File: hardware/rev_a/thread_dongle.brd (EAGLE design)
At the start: 26 x 14 mm, 26 parts, among them J1 USB-A-MALE-PLUG, J2 TC2030-JLINK-NL, U2 ESDR0502N, U3 CP2102, Y1 FH1600015

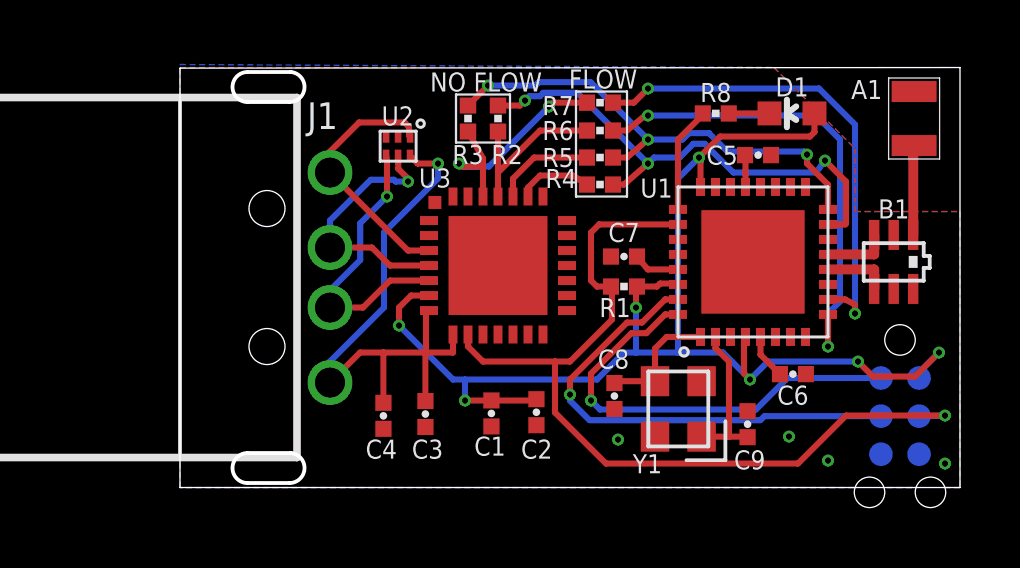
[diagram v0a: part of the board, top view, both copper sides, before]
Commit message: smaller board, cheaper uart bridge
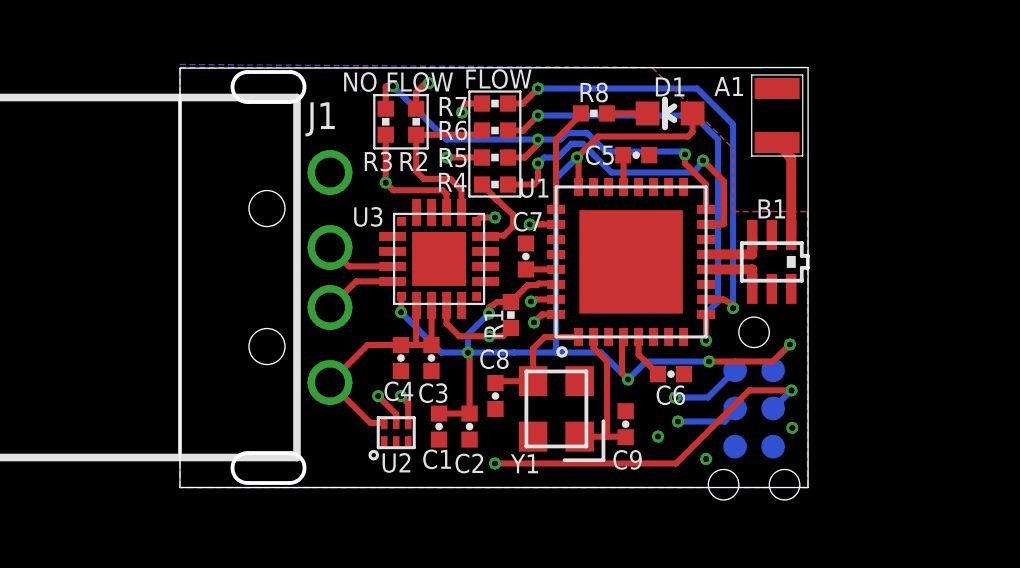
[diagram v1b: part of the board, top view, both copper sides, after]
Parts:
- U3: value CP2102 -> CP2102N-20; device silabs:MLP28 -> chips:QFN-20-3MM
- moved U2 9.55 mm to (7.21, 1.83), turned to 90 degrees
- moved J2 4.87 mm to (19.1, 2.63)
- moved A1 4.57 mm to (19.9, 11.2)
- moved C9 4.06 mm to (14.9, 2.11)
- moved U1 4.06 mm to (15.0, 7.52)
- moved B1 4.06 mm to (19.7, 7.52)
- moved C5 4.06 mm to (15.2, 11.1)
- moved C6 4.06 mm to (16.4, 3.78)
- moved D1 4.06 mm to (16.3, 12.5)
- moved R8 4.06 mm to (13.8, 12.5)
- moved Y1 4.06 mm to (12.5, 2.62)
- moved C8 3.96 mm to (10.5, 3.05)
- moved R1 3.89 mm to (11.0, 5.75), turned to 90 degrees
- moved R7 3.50 mm to (10.5, 12.8)
- moved R4 3.50 mm to (10.5, 10.1)
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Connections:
- net GND: now also U3.12, U3.P$1; no longer U3.EXP, U3.M
- net SAM_CTS: now also U3.16; no longer U3.24
- net SAM_RTS: now also U3.15; no longer U3.23
- net SAM_RX: now also U3.18; no longer U3.26
- net SAM_TX: now also U3.17; no longer U3.25
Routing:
- net N$6: track 19.7 -> 8.91 mm, vias 1 -> 0
- net GND: track 8.52 -> 0.00 mm, vias 4 -> 3
- net VCC: track 44.2 -> 37.7 mm
- net !RESET: track 29.4 -> 24.4 mm, vias 1 -> 4
- net SWDIO: track 14.8 -> 10.8 mm, vias 1 -> 2
- net SWCLK: track 16.1 -> 12.5 mm, vias 1 -> 2
- net N$4: track 9.52 -> 7.37 mm
- net SAM_CTS: track 3.36 -> 4.50 mm, vias 0 -> 2
- net SER2_P3: track 16.3 -> 15.4 mm
- net SER2_P0: track 16.2 -> 15.4 mm
- net SAM_RTS: track 2.52 -> 3.31 mm
- net SER2_P1: track 16.3 -> 15.5 mm
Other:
- board size 26 x 14 mm -> 20.9 x 14 mm
- board text removed: "U3"

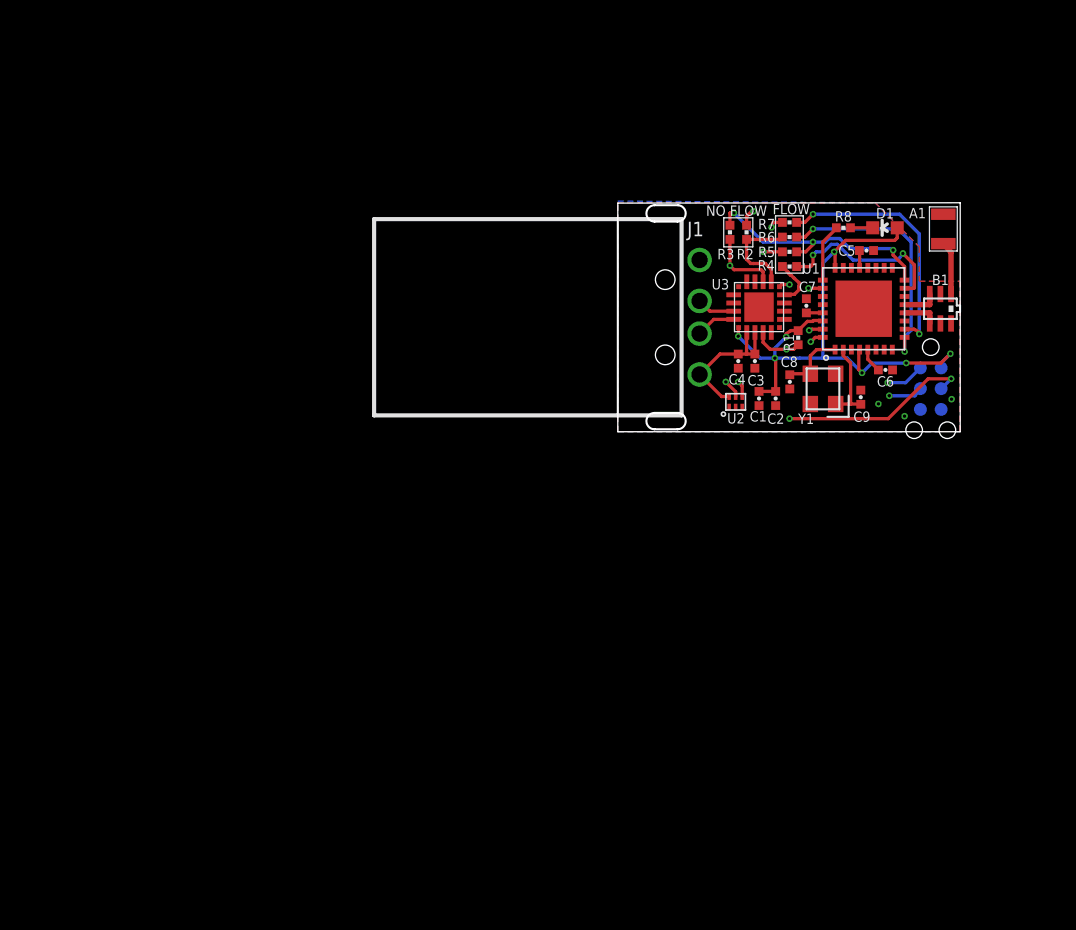
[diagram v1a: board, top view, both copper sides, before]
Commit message: Update with KW21Z instead of SAMR21
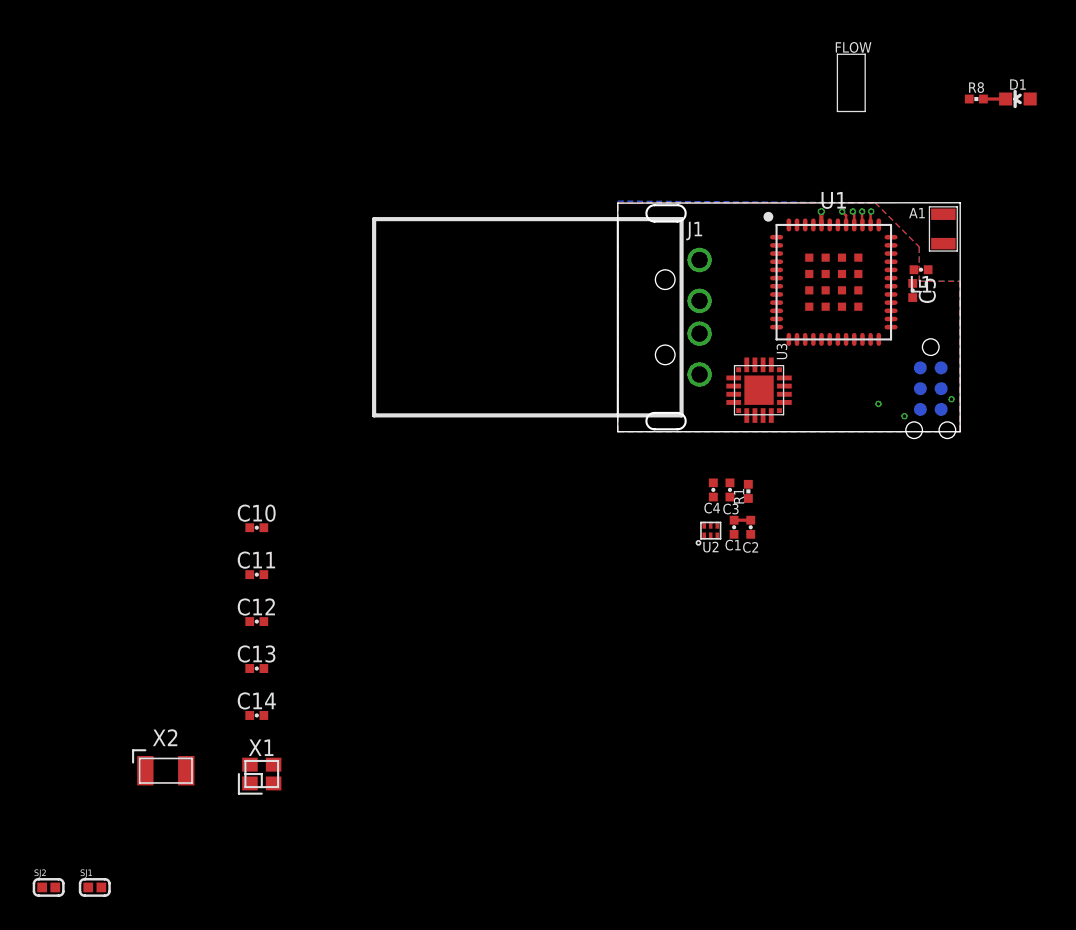
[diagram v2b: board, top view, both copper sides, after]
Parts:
- removed B1: 2450BM15A0015, chips:2450BM
- removed C6: 0.1uF, passives:0402_CAP
- removed C7: 1.0uF, passives:0402_CAP
- removed C8, C9: 8pF, passives:0402_CAP
- removed R2, R3, R4, R5, R6, R7: 0, passives:0402_RES
- removed Y1: FH1600015, crystals:FHXXX
- added C10, C11, C12: 0.1uF, passives:0402_CAP
- added C13, C14: 12pF, passives:0402_CAP
- added L1: (no value), passives:0402_CAP
- added SJ1, SJ2: SOLDERJUMPERNC, headers:SJ_2S_SMALL
- added X1: FA-128, crystals:FA-128
- added X2: FA-135, crystals:FC-135
- C5: value 0.1uF -> 0.7pF
- U1: value (none) -> KW21Z; device chips:UQFN-32 -> chips:LAMINATE-QFN-48-7MM
- moved D1 11.3 mm to (24.5, 20.3)
- moved R8 11.3 mm to (21.9, 20.3)
- moved R1 9.88 mm to (7.98, -3.65)
- moved C3 8.02 mm to (6.86, -3.56)
- moved C4 8.02 mm to (5.84, -3.56)
- moved U2 8.02 mm to (5.68, -6.05)
- moved C1 8.02 mm to (7.11, -5.84)
- moved C2 8.02 mm to (8.13, -5.84)
- moved U3 5.08 mm to (8.64, 2.54), turned to 270 degrees
- moved C5 3.74 mm to (18.0, 8.64), turned to 270 degrees
- moved U1 2.45 mm to (13.2, 9.14), turned to 0 degrees
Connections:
- net N$4 renamed D-
- net N$5 renamed D+
- net N$6 renamed 5V
- removed net N$1: B1.4, U1.12
- removed net N$10: C8.1, U1.1, Y1.3
- removed net N$17: C7.1, U1.29
- removed net N$2: B1.3, U1.13
- removed net N$3: A1.P1, B1.1
- removed net N$9: C9.1, U1.2, Y1.1
- removed net SAM_CTS: R5.2, U3.16
- removed net SAM_RTS: R4.2, U3.15
- removed net SAM_RX: R3.2, R7.2, U3.18
- removed net SAM_TX: R2.2, R6.2, U3.17
- removed net SER1_P2_DBG_RX: U1.20
- removed net SER1_P2_DBG_TX: U1.19
- removed net SER2_P0: R6.1, U1.9
- removed net SER2_P1: R7.1, U1.10
- removed net SER2_P2: R2.1, R4.1, U1.15
- removed net SER2_P3: R3.1, R5.1, U1.16
- new net CP_CTS: SJ2.2, U3.15
- new net CP_RTS: SJ1.2, U3.16
- new net KW21Z_CTS: SJ1.1, U1.40
- new net KW21Z_RTS: SJ2.1, U1.41
- new net KW21Z_RX: U1.38, U3.18
- new net KW21Z_TX: U1.39, U3.17
- new net N$11: U1.30, X1.3
- new net N$12: U1.31, X1.1
- new net N$13: C5.1, L1.2, U1.33
- new net N$14: U1.22, X2.1
- net !RESET: now also U1.3; no longer U1.26
- net GND: now also C10.2, C11.2, C12.2, C13.2, C14.2, U1.13, U1.26, U1.34, U1.49, U1.50, U1.51, U1.52, U1.53, U1.54, U1.55, U1.56, U1.57, U1.58, U1.59, U1.60, U1.61, U1.62, U1.63, U1.64, U1.8, X1.2, X1.4; no longer B1.2, B1.5, B1.6, C6.2, C7.2, C8.2, C9.2, U1.11, U1.14, U1.18, U1.28, U1.3, U1.6, U1.THERMAL
- net N$15: now also X2.2; no longer C5.1
- net N$16: now also A1.P1, L1.1; no longer C6.1, U1.5
- net N$8: now also U1.16; no longer U1.25
- net SWCLK: now also U1.1; no longer U1.31
- net SWDIO: now also U1.2; no longer U1.32
- net VCC: now also C10.1, C11.1, C12.1, C13.1, C14.1, U1.10, U1.14, U1.15, U1.20, U1.27, U1.28, U1.32, U1.35, U1.36, U1.44, U1.9; no longer U1.24, U1.30, U1.4
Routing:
- net VCC: track 37.7 -> 1.94 mm, vias 7 -> 1
- net !RESET: track 24.4 -> 0.00 mm, vias 4 -> 0
- net SER2_P2: track 16.9 -> 0.00 mm, vias 3 -> 0
- net SER2_P1: track 15.5 -> 0.00 mm, vias 2 -> 0
- net SER2_P3: track 15.4 -> 0.00 mm, vias 3 -> 0
- net SER2_P0: track 15.4 -> 0.00 mm, vias 2 -> 0
- net SWCLK: track 12.5 -> 0.00 mm, vias 2 -> 0
- net SWDIO: track 10.8 -> 0.00 mm, vias 2 -> 0
- net D+: track 9.11 -> 0.00 mm, vias 1 -> 0
- net 5V: track 8.91 -> 0.00 mm
- net SAM_RX: track 8.80 -> 0.00 mm, vias 2 -> 0
- net D-: track 7.37 -> 0.00 mm, vias 1 -> 0
- net SAM_TX: track 5.97 -> 0.00 mm
- net N$9: track 5.05 -> 0.00 mm
- net SAM_CTS: track 4.50 -> 0.00 mm, vias 2 -> 0
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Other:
- board text removed: "NO FLOW"

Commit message: Nothing to do and no errors
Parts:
- added C6, C7: 12pF, passives:0402_CAP
- moved SJ2 56.3 mm to (13.8, 0.72), turned to 180 degrees
- moved SJ1 54.5 mm to (13.8, 1.71), turned to 180 degrees
- moved X2 49.1 mm to (15.0, 3.56), turned to 180 degrees
- moved X1 48.9 mm to (18.3, 7.11), turned to 90 degrees
- moved C14 48.4 mm to (16.4, 12.1), turned to 90 degrees
- moved C13 47.1 mm to (15.9, 13.3)
- moved C12 41.8 mm to (16.3, 5.08)
- moved C11 36.5 mm to (6.99, 13.3), turned to 180 degrees
- moved C10 34.8 mm to (11.2, 4.57), turned to 180 degrees
- moved U2 18.0 mm to (6.49, 12.0), turned to 270 degrees
- moved D1 17.8 mm to (20.1, 3.05), turned to 180 degrees
- moved R8 17.6 mm to (18.8, 3.05), turned to 270 degrees
- moved C1 15.1 mm to (7.24, 9.27), turned to 90 degrees
- moved C2 13.9 mm to (6.86, 8.00), turned to 180 degrees
- moved C4 7.13 mm to (6.35, 3.56), turned to 90 degrees
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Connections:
- removed net N$11: U1.30, X1.3
- removed net N$14: U1.22, X2.1
- removed net N$15: U1.21, X2.2
- new net N$1: C6.1, U1.21, X2.2
- new net N$2: C7.1, U1.22, X2.1
- new net N$3: U1.31, X1.3
- net GND: now also C6.2, C7.2
- net N$12: now also U1.30; no longer U1.31
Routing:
- net !RESET: track 0.00 -> 31.3 mm, vias 0 -> 3
- net VCC: track 1.94 -> 29.0 mm, vias 1 -> 9
- net SWCLK: track 0.00 -> 19.1 mm, vias 0 -> 2
- net SWDIO: track 0.00 -> 17.4 mm, vias 0 -> 1
- net KW21Z_RTS: track 0.92 -> 16.5 mm, vias 1 -> 3
- net 5V: track 0.00 -> 15.2 mm, vias 0 -> 1
- net KW21Z_RX: track 0.83 -> 15.6 mm, vias 1 -> 2
- net KW21Z_CTS: track 0.85 -> 15.6 mm, vias 1 -> 3
- net KW21Z_TX: track 0.83 -> 14.7 mm, vias 1 -> 2
- net D-: track 0.00 -> 12.8 mm
- net N$8: track 0.08 -> 10.8 mm, vias 0 -> 2
- net D+: track 0.00 -> 10.1 mm
- net GND: track 0.00 -> 8.87 mm, vias 3 -> 47
- net N$12: track 0.00 -> 6.43 mm
- net N$2: track 0.00 -> 5.27 mm
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- added copper zone on layer 15, net VCC
- removed copper zone on layer 15, net GND
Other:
- board size 20.9 x 14 mm -> 22 x 14 mm

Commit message: Fix up silkscreen
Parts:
- moved SJ2 0.10 mm to (13.7, 0.64)
- moved SJ1 0.08 mm to (13.7, 1.65)
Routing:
- net CP_CTS: track 3.52 -> 0.20 mm
- net KW21Z_CTS: track 15.6 -> 14.0 mm
- net KW21Z_RTS: track 16.5 -> 15.3 mm
- net CP_RTS: track 3.19 -> 2.42 mm

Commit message: ship it
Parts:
- removed C13, C14: 12pF, passives:0402_CAP
- removed R8: 1k, passives:0402_RES
- added C8, C9: 0.1uF, passives:0402_CAP
- added R2: 10k, passives:0402_RES
- C1: value 0.1uF -> 0.7pF
- C11: value 0.1uF -> 1.0uF
- C12: value 0.1uF -> 4.7uF
- C2: value 4.7uF -> 12pF
- C3: value 0.1uF -> 12pF
- C4: value 1.0uF -> 12pF
- C5: value 0.7pF -> 12pF
- C6, C7: value 12pF -> 0.1uF
- J1: value USB-A-MALE-PLUG -> TC2030-JLINK-NL; device connector:USB_A_MALE_PLUG_CUI_UP2-AH -> connector:TC2030-IDC-NL
- J2: value TC2030-JLINK-NL -> USB-A-MALE-PLUG; device connector:TC2030-IDC-NL -> connector:USB_A_MALE_PLUG_CUI_UP2-AH
- R1: value 10k -> 1k
- U1: value KW21Z -> CP2102N-20; device chips:LAMINATE-QFN-48-7MM -> chips:QFN-20-3MM
- U3: value CP2102N-20 -> KW21Z; device chips:QFN-20-3MM -> chips:LAMINATE-QFN-48-7MM
- moved J1 20.5 mm to (20.1, 3.40), flipped to the bottom
- moved J2 20.5 mm to (0.00, 7.00), flipped to the top
- moved C3 15.2 mm to (16.4, 12.2), turned to 90 degrees
- moved R1 12.6 mm to (18.8, 3.05)
- moved C7 12.5 mm to (5.08, 2.03), turned to 180 degrees
- moved C2 10.5 mm to (15.9, 13.3), turned to 0 degrees
- moved C1 10.4 mm to (17.4, 11.6)
- moved C12 9.84 mm to (6.86, 8.00), turned to 180 degrees
- moved C11 9.80 mm to (6.35, 3.56), turned to 90 degrees
- moved C5 8.00 mm to (17.4, 3.56)
- moved C6 7.73 mm to (6.86, 8.89), turned to 180 degrees
- moved U1 7.33 mm to (9.14, 2.41), turned to 270 degrees
- moved U3 7.33 mm to (11.9, 9.20), turned to 0 degrees
- moved C4 6.10 mm to (12.4, 3.56)
- moved C10 5.11 mm to (16.3, 5.08), turned to 0 degrees
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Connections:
- removed net SWCLK: J2.4, U1.1
- new net SWDCLK: J1.4, U3.2
- net !RESET: now also J1.3, R2.1, U1.9, U3.3; no longer J2.3, R1.1, U1.3, U3.9
- net 5V: now also C11.1, C7.1, J2.P$1, U1.7, U1.8; no longer C3.1, C4.1, J1.P$1, U3.7, U3.8
- net CP_CTS: now also U1.15; no longer U3.15
- net CP_RTS: now also U1.16; no longer U3.16
- net D+: now also J2.P$3, U1.4; no longer J1.P$3, U3.4
- net D-: now also J2.P$2, U1.5; no longer J1.P$2, U3.5
- net GND: now also C8.2, C9.2, J1.5, J2.P$4, U1.12, U1.3, U1.P$1, U3.13, U3.26, U3.34, U3.49, U3.50, U3.51, U3.52, U3.53, U3.54, U3.55, U3.56, U3.57, U3.58, U3.59, U3.60, U3.61, U3.62, U3.63, U3.64, U3.8; no longer C13.2, C14.2, J1.P$4, J2.5, U1.13, U1.26, U1.34, U1.49, U1.50, U1.51, U1.52, U1.53, U1.54, U1.55, U1.56, U1.57, U1.58, U1.59, U1.60, U1.61, U1.62, U1.63, U1.64, U1.8, U3.12, U3.3, U3.P$1
- net KW21Z_CTS: now also U3.40; no longer U1.40
- net KW21Z_RTS: now also U3.41; no longer U1.41
- net KW21Z_RX: now also U1.18, U3.38; no longer U1.38, U3.18
- net KW21Z_TX: now also U1.17, U3.39; no longer U1.39, U3.17
- net N$1: now also C4.1, U3.21; no longer C6.1, U1.21
- net N$12: now also U3.30; no longer U1.30
- net N$13: now also C1.1, U3.33; no longer C5.1, U1.33
- net N$2: now also C5.1, U3.22; no longer C7.1, U1.22
- net N$3: now also U3.31; no longer U1.31
- net N$7: now also R1.2; no longer R8.2
- net N$8: now also R1.1, U3.16; no longer R8.1, U1.16
- net SWDIO: now also J1.2, U3.1; no longer J2.2, U1.2
- net VCC: now also C3.1, C6.1, C8.1, C9.1, J1.1, R2.2, U1.6, U3.10, U3.14, U3.15, U3.20, U3.27, U3.28, U3.32, U3.35, U3.36, U3.44, U3.9; no longer C1.1, C11.1, C13.1, C14.1, J2.1, R1.2, U1.10, U1.14, U1.15, U1.20, U1.27, U1.28, U1.32, U1.35, U1.36, U1.44, U1.9, U3.6
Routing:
- net SWCLK: track 19.1 -> 0.00 mm, vias 2 -> 0
- net SWDCLK: track 0.00 -> 18.9 mm, vias 0 -> 1
- net GND: track 8.87 -> 12.3 mm, vias 47 -> 46
- net CP_CTS: track 0.20 -> 3.52 mm
- net KW21Z_TX: track 14.7 -> 13.3 mm
- net KW21Z_RTS: track 15.3 -> 14.3 mm
- net KW21Z_RX: track 15.6 -> 14.7 mm
- net CP_RTS: track 2.42 -> 3.12 mm
- net SWDIO: track 17.4 -> 18.0 mm
